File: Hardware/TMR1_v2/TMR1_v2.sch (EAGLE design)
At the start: 53 parts, among them J1 455-1750-1-ND, J2 455-1750-1-ND, U1 ATMEGA328P_TQFP, U2 MCP79410I/SN, Y1 32.768kHz

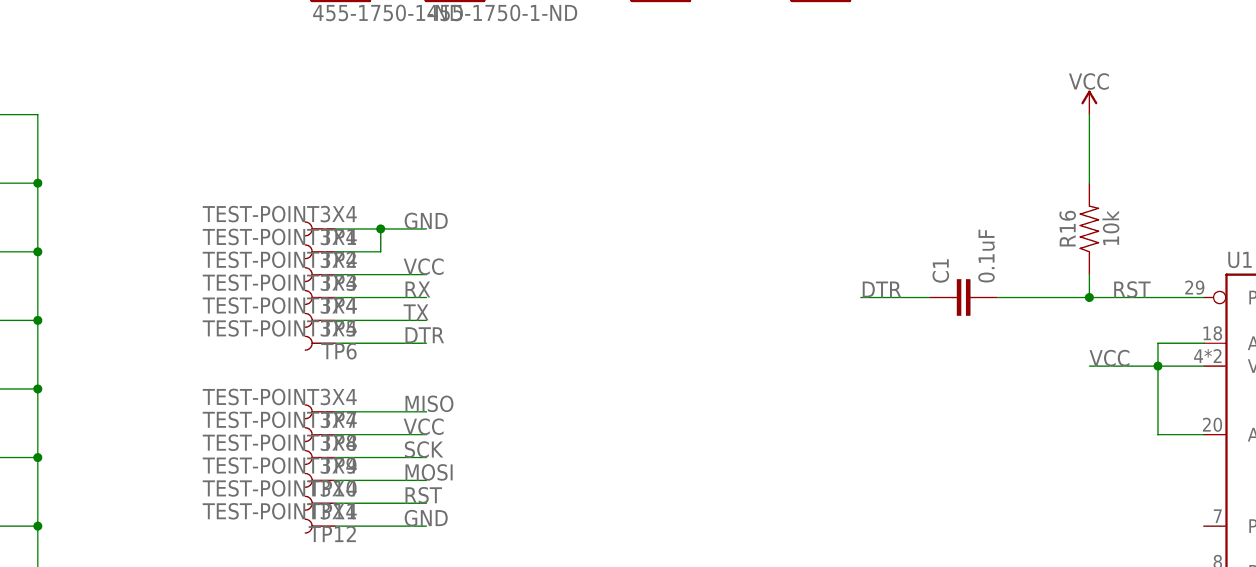
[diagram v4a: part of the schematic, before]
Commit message: PCB finished and Gerbers generated
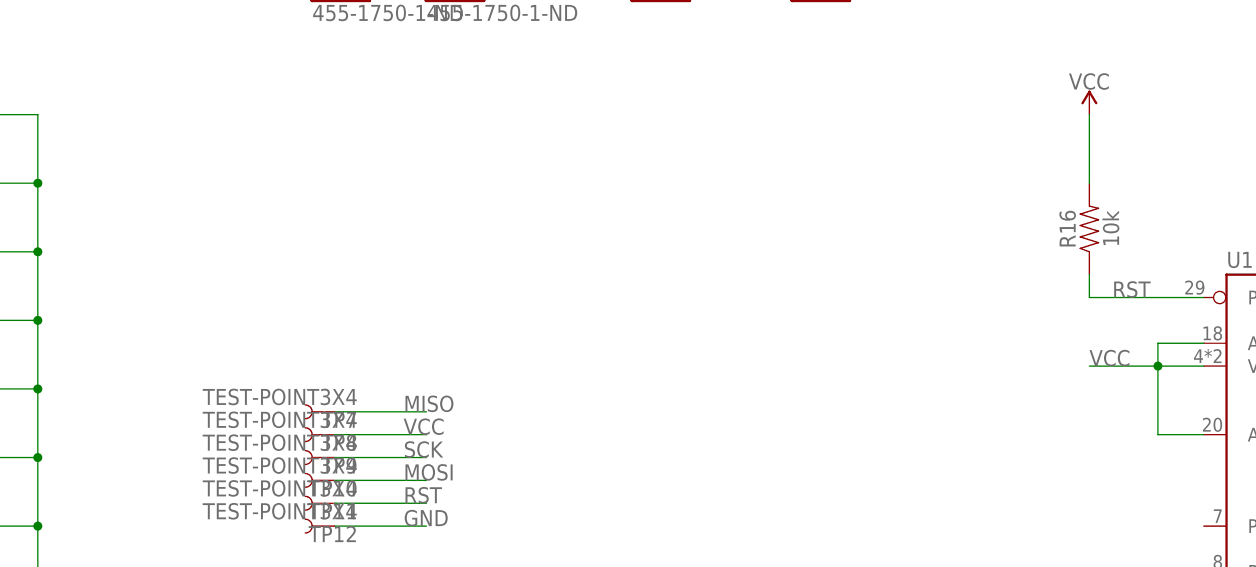
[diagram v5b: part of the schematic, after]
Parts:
- removed C1: 0.1uF, SparkFun-Capacitors:0.1UF-0402-16V-10%
- removed TP1, TP2, TP3, TP4, TP5, TP6: TEST-POINT3X4, SparkFun-Connectors:TEST-POINT3X4
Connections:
- removed net DTR: C1.1, TP6.1
- net GND: no longer TP1.1, TP2.1
- net RST: no longer C1.2
- net RX: no longer TP4.1
- net TX: no longer TP5.1
- net VCC: no longer TP3.1
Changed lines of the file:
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@@
 <parts>
 <part name="U1" library="SparkFun-IC-Microcontroller" deviceset="ATMEGA328P_TQFP" device="" value="ATMEGA328P_TQFP"/>
-<part name="C1" library="SparkFun-Capacitors" deviceset="0.1UF" device="-0402-16V-10%" value="0.1uF"/>
 <part name="SUPPLY1" library="SparkFun-PowerSymbols" deviceset="VCC" device=""/>
 <part name="SUPPLY2" library="SparkFun-PowerSymbols" deviceset="VCC" device=""/>
@@
 <part name="SUPPLY4" library="SparkFun-PowerSymbols" deviceset="VCC" device=""/>
 <part name="SUPPLY5" library="SparkFun-PowerSymbols" deviceset="VCC" device=""/>
-<part name="TP1" library="SparkFun-Connectors" deviceset="TEST-POINT" device="3X4"/>
-<part name="TP2" library="SparkFun-Connectors" deviceset="TEST-POINT" device="3X4"/>
-<part name="TP3" library="SparkFun-Connectors" deviceset="TEST-POINT" device="3X4"/>
-<part name="TP4" library="SparkFun-Connectors" deviceset="TEST-POINT" device="3X4"/>
-<part name="TP5" library="SparkFun-Connectors" deviceset="TEST-POINT" device="3X4"/>
-<part name="TP6" library="SparkFun-Connectors" deviceset="TEST-POINT" device="3X4"/>
 <part name="S1" library="SparkFun-Switches" deviceset="MOMENTARY-SWITCH-SPST" device="-SMD-5.2MM"/>
 <part name="R1" library="SparkFun-Resistors" deviceset="330OHM" device="-0603-1/10W-1%" value="330"/>
@@
 <attribute name="VALUE" x="182.88" y="91.44" size="1.778" layer="96"/>
 </instance>
-<instance part="C1" gate="G$1" x="154.94" y="154.94" rot="R90">
-<attribute name="NAME" x="152.019" y="156.464" size="1.778" layer="95" font="vector" rot="R90"/>
-<attribute name="VALUE" x="157.099" y="156.464" size="1.778" layer="96" font="vector" rot="R90"/>
-</instance>
 <instance part="SUPPLY1" gate="G$1" x="167.64" y="175.26">
 <attribute name="VALUE" x="167.64" y="178.054" size="1.778" layer="96" align="bottom-center"/>
@@
 <instance part="SUPPLY5" gate="G$1" x="121.92" y="53.34">
 <attribute name="VALUE" x="121.92" y="56.134" size="1.778" layer="96" align="bottom-center"/>
-</instance>
-<instance part="TP1" gate="G$1" x="83.82" y="162.56" rot="R180">
-<attribute name="NAME" x="86.36" y="162.56" size="1.778" layer="95" font="vector" rot="R180"/>
-</instance>
-<instance part="TP2" gate="G$1" x="83.82" y="160.02" rot="R180">
-<attribute name="NAME" x="86.36" y="160.02" size="1.778" layer="95" font="vector" rot="R180"/>
-</instance>
-<instance part="TP3" gate="G$1" x="83.82" y="157.48" rot="R180">
-<attribute name="NAME" x="86.36" y="157.48" size="1.778" layer="95" font="vector" rot="R180"/>
-</instance>
-<instance part="TP4" gate="G$1" x="83.82" y="154.94" rot="R180">
-<attribute name="NAME" x="86.36" y="154.94" size="1.778" layer="95" font="vector" rot="R180"/>
-</instance>
-<instance part="TP5" gate="G$1" x="83.82" y="152.4" rot="R180">
-<attribute name="NAME" x="86.36" y="152.4" size="1.778" layer="95" font="vector" rot="R180"/>
-</instance>
-<instance part="TP6" gate="G$1" x="83.82" y="149.86" rot="R180">
-<attribute name="NAME" x="86.36" y="149.86" size="1.778" layer="95" font="vector" rot="R180"/>
 </instance>
 <instance part="S1" gate="G$1" x="88.9" y="106.68">
@@
 </segment>
 <segment>
-<label x="91.44" y="162.56" size="1.778" layer="95"/>
-<wire x1="88.9" y1="162.56" x2="93.98" y2="162.56" width="0.1524" layer="91"/>
-<wire x1="88.9" y1="160.02" x2="88.9" y2="162.56" width="0.1524" layer="91"/>
-<junction x="88.9" y="162.56"/>
-<wire x1="83.82" y1="162.56" x2="88.9" y2="162.56" width="0.1524" layer="91"/>
-<wire x1="83.82" y1="160.02" x2="88.9" y2="160.02" width="0.1524" layer="91"/>
-<pinref part="TP1" gate="G$1" pin="1"/>
-<pinref part="TP2" gate="G$1" pin="1"/>
-</segment>
-<segment>
 <pinref part="GND4" gate="1" pin="GND"/>
 <wire x1="91.44" y1="88.9" x2="91.44" y2="91.44" width="0.1524" layer="91"/>
@@
 </segment>
 <segment>
-<wire x1="83.82" y1="157.48" x2="93.98" y2="157.48" width="0.1524" layer="91"/>
-<label x="91.44" y="157.48" size="1.778" layer="95"/>
-<pinref part="TP3" gate="G$1" pin="1"/>
-</segment>
-<segment>
 <pinref part="SUPPLY3" gate="G$1" pin="VCC"/>
 <wire x1="76.2" y1="111.76" x2="76.2" y2="106.68" width="0.1524" layer="91"/>
@@
 <segment>
 <pinref part="U1" gate="U1" pin="PC6(/RESET)"/>
-<pinref part="C1" gate="G$1" pin="2"/>
 <wire x1="180.34" y1="154.94" x2="167.64" y2="154.94" width="0.1524" layer="91"/>
-<wire x1="167.64" y1="154.94" x2="157.48" y2="154.94" width="0.1524" layer="91"/>
 <wire x1="167.64" y1="157.48" x2="167.64" y2="154.94" width="0.1524" layer="91"/>
-<junction x="167.64" y="154.94"/>
 <label x="170.18" y="154.94" size="1.778" layer="95"/>
 <pinref part="R16" gate="G$1" pin="1"/>
@@
 </segment>
 </net>
-<net name="DTR" class="0">
-<segment>
-<pinref part="C1" gate="G$1" pin="1"/>
-<wire x1="149.86" y1="154.94" x2="142.24" y2="154.94" width="0.1524" layer="91"/>
-<label x="142.24" y="154.94" size="1.778" layer="95"/>
-</segment>
-<segment>
-<wire x1="83.82" y1="149.86" x2="93.98" y2="149.86" width="0.1524" layer="91"/>
-<label x="91.44" y="149.86" size="1.778" layer="95"/>
-<pinref part="TP6" gate="G$1" pin="1"/>
-</segment>
-</net>
 <net name="N$18" class="0">
 <segment>
@@
 <label x="228.6" y="132.08" size="1.778" layer="95"/>
 </segment>
-<segment>
-<wire x1="83.82" y1="154.94" x2="93.98" y2="154.94" width="0.1524" layer="91"/>
-<label x="91.44" y="154.94" size="1.778" layer="95"/>
-<pinref part="TP4" gate="G$1" pin="1"/>
-</segment>
 </net>
 <net name="TX" class="0">
@@
 <label x="228.6" y="129.54" size="1.778" layer="95"/>
 </segment>
-<segment>
-<wire x1="83.82" y1="152.4" x2="93.98" y2="152.4" width="0.1524" layer="91"/>
-<label x="91.44" y="152.4" size="1.778" layer="95"/>
-<pinref part="TP5" gate="G$1" pin="1"/>
-</segment>
-</net>
+</net>

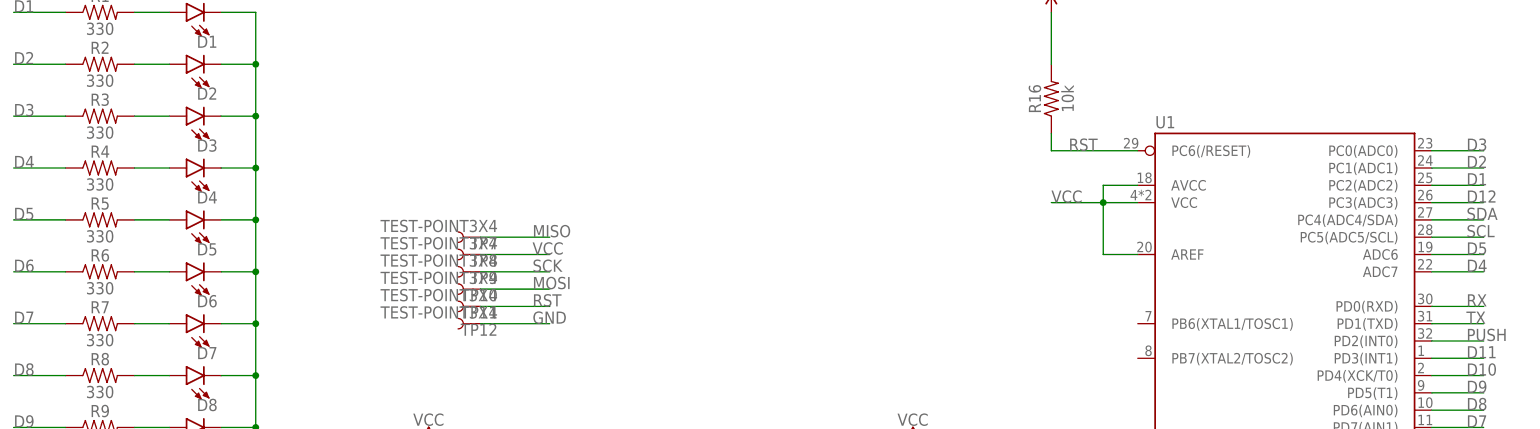
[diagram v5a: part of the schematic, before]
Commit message: correction for the analogic pings ADC6-7 with MISO-SCK, HW and SW
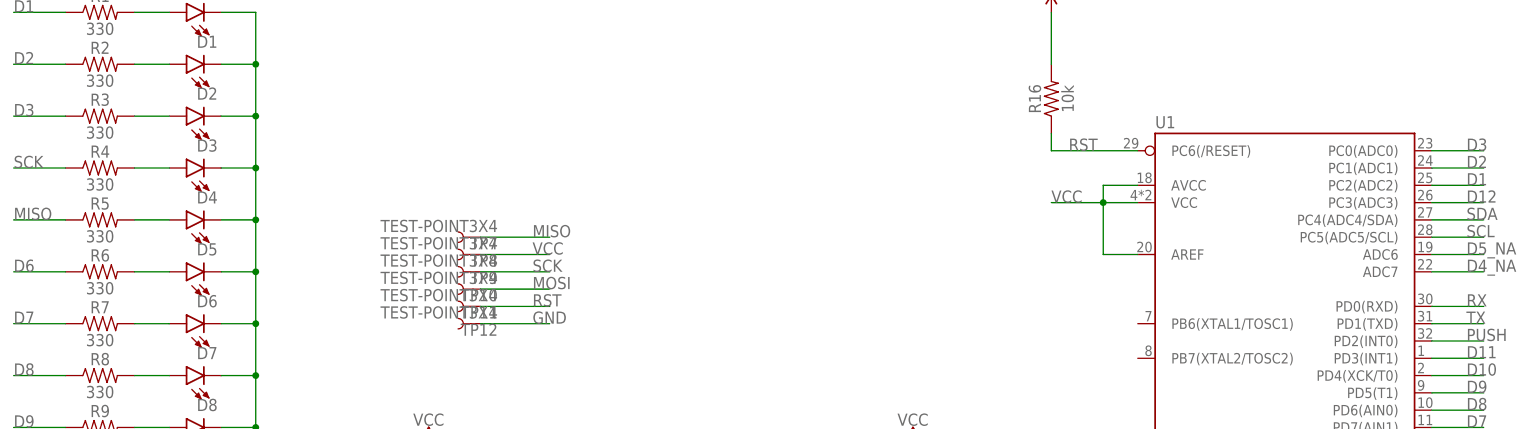
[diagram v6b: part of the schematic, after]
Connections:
- removed net D4: R4.1, U1.ADC7
- removed net D5: R5.1, U1.ADC6
- new net D4_NA: U1.ADC7
- new net D5_NA: U1.ADC6
- net MISO: now also R5.1
- net SCK: now also R4.1
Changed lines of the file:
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@@
 <setting verticaltext="up"/>
 </settings>
-<grid distance="0.1" unitdist="inch" unit="inch" style="lines" multiple="1" display="no" altdistance="0.01" altunitdist="inch" altunit="inch"/>
+<grid distance="0.1" unitdist="inch" unit="inch" style="lines" multiple="1" display="yes" altdistance="0.01" altunitdist="inch" altunit="inch"/>
 <layers>
 <layer number="1" name="Top" color="4" fill="1" visible="no" active="no"/>
@@
 <pinref part="TP7" gate="G$1" pin="1"/>
 </segment>
+<segment>
+<wire x1="22.86" y1="144.78" x2="15.24" y2="144.78" width="0.1524" layer="91"/>
+<label x="15.24" y="144.78" size="1.778" layer="95"/>
+<pinref part="R5" gate="G$1" pin="1"/>
+</segment>
 </net>
 <net name="SCK" class="0">
@@
 <pinref part="TP9" gate="G$1" pin="1"/>
 </segment>
+<segment>
+<wire x1="22.86" y1="152.4" x2="15.24" y2="152.4" width="0.1524" layer="91"/>
+<label x="15.24" y="152.4" size="1.778" layer="95"/>
+<pinref part="R4" gate="G$1" pin="1"/>
+</segment>
 </net>
 <net name="D1" class="0">
@@
 </segment>
 </net>
-<net name="D4" class="0">
-<segment>
-<wire x1="22.86" y1="152.4" x2="15.24" y2="152.4" width="0.1524" layer="91"/>
-<label x="15.24" y="152.4" size="1.778" layer="95"/>
-<pinref part="R4" gate="G$1" pin="1"/>
-</segment>
+<net name="D4_NA" class="0">
 <segment>
 <pinref part="U1" gate="U1" pin="ADC7"/>
 <wire x1="223.52" y1="137.16" x2="231.14" y2="137.16" width="0.1524" layer="91"/>
 <label x="228.6" y="137.16" size="1.778" layer="95"/>
-</segment>
-</net>
-<net name="D5" class="0">
-<segment>
-<wire x1="22.86" y1="144.78" x2="15.24" y2="144.78" width="0.1524" layer="91"/>
-<label x="15.24" y="144.78" size="1.778" layer="95"/>
-<pinref part="R5" gate="G$1" pin="1"/>
-</segment>
-<segment>
-<pinref part="U1" gate="U1" pin="ADC6"/>
-<wire x1="223.52" y1="139.7" x2="231.14" y2="139.7" width="0.1524" layer="91"/>
-<label x="228.6" y="139.7" size="1.778" layer="95"/>
 </segment>
 </net>
@@
 </segment>
 </net>
+<net name="D5_NA" class="0">
+<segment>
+<pinref part="U1" gate="U1" pin="ADC6"/>
+<wire x1="223.52" y1="139.7" x2="231.14" y2="139.7" width="0.1524" layer="91"/>
+<label x="228.6" y="139.7" size="1.778" layer="95"/>
+</segment>
+</net>
